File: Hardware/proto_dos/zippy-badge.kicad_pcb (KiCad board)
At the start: 2 copper layers, 98 x 104 mm, 90 parts, among them J1 Micro_SD_Card_SPI, J2 USB-C, SW1 Boot Select, SW2 SW_SPDT, U1 NCP115ASN330T2G, U2 RP2040, U3 W25Q32RV, X1 Badgelife_sao_connector_v169b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, Y1 ABM8-272-T3

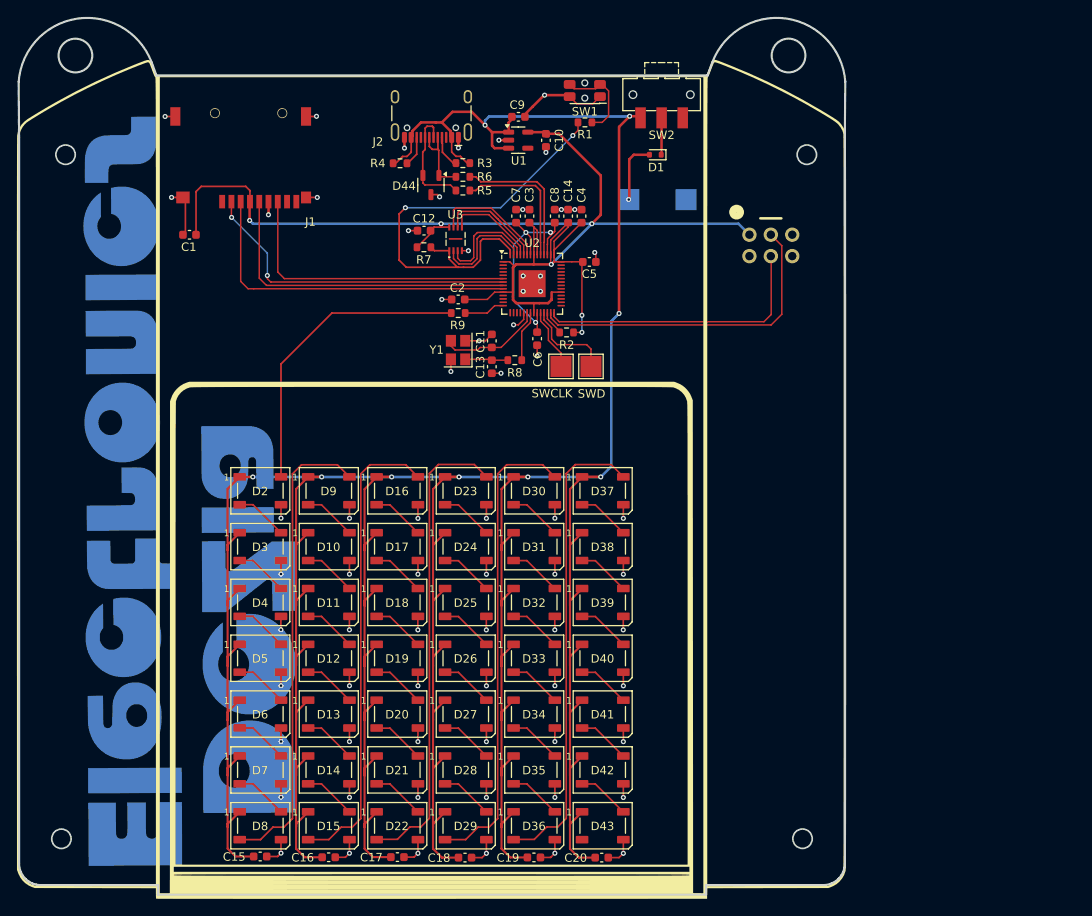
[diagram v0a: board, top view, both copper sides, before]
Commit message: Updated schematic to add Flipper Zero GPIO pinout Modified pin out of RP2040 to make for better routing Update of PCB to add new parts and test layout
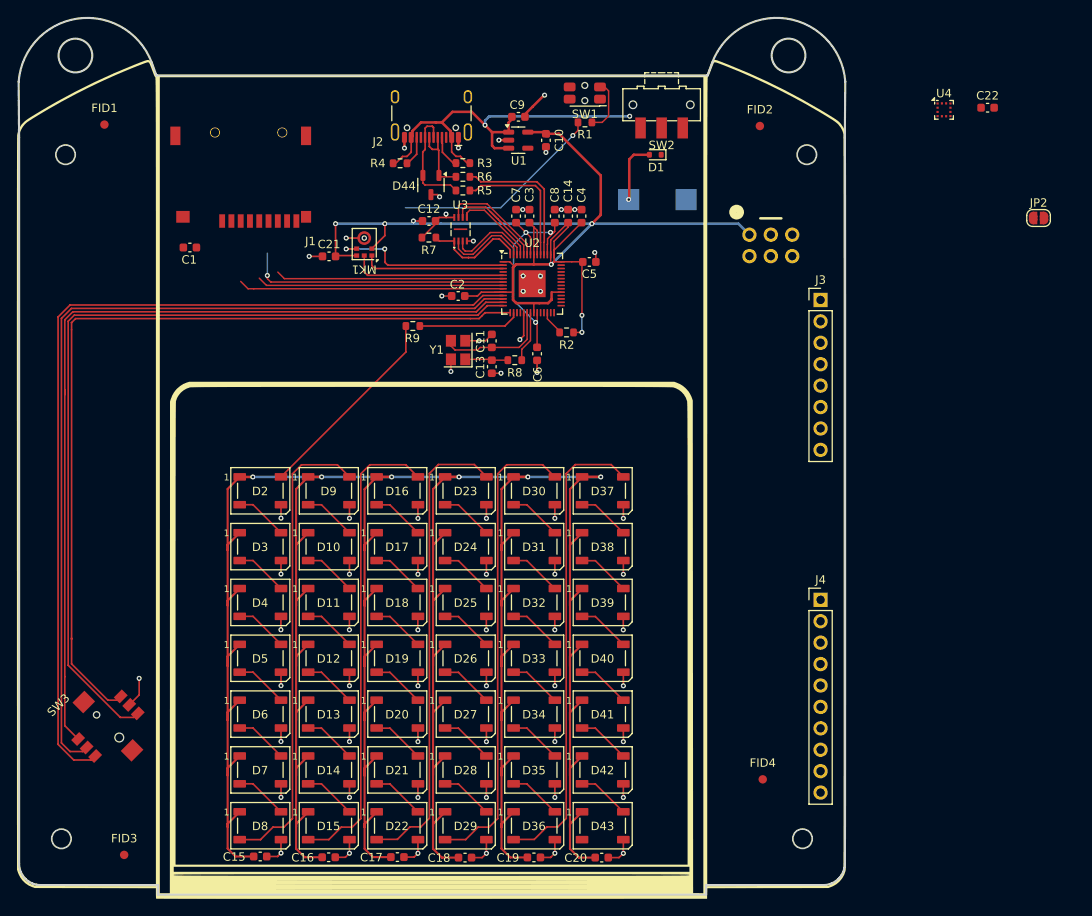
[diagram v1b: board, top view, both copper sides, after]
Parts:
- removed the G*** at (133.9, 91.4)
- removed TP3: SWCLK, TestPoint:TestPoint_Pad_2.5x2.5mm
- removed TP4: SWD, TestPoint:TestPoint_Pad_2.5x2.5mm
- added C21: 0.1uF, Capacitor_SMD:C_0603_1608Metric, F.Cu at (118.2, 63.3)
- added C22: 0.1uF, Capacitor_SMD:C_0603_1608Metric, F.Cu at (196.3, 45.6)
- added FID1: Fiducial, Fiducial:Fiducial_1mm_Mask2mm, F.Cu at (91.5, 47.6)
- added FID2: Fiducial, Fiducial:Fiducial_1mm_Mask2mm, F.Cu at (169.3, 47.8)
- added FID3: Fiducial, Fiducial:Fiducial_1mm_Mask2mm, F.Cu at (93.9, 134.2)
- added FID4: Fiducial, Fiducial:Fiducial_1mm_Mask2mm, F.Cu at (169.6, 125.3)
- added J3: Conn_01x08, Connector_PinHeader_2.54mm:PinHeader_1x08_P2.54mm_Vertical, F.Cu at (176.5, 68.4)
- added J4: Conn_01x10, Connector_PinHeader_2.54mm:PinHeader_1x10_P2.54mm_Vertical, F.Cu at (176.5, 104.0)
- added JP2: SolderJumper_2_Open, Jumper:SolderJumper-2_P1.3mm_Open_RoundedPad1.0x1.5mm, F.Cu at (202.3, 58.7)
- added MK1: ICS-43434, Sensor_Audio:InvenSense_ICS-43434-6_3.5x2.65mm, F.Cu at (122.3, 61.8)
- added SW3: SKRHABE010, lib_fp:SKRHABE010, F.Cu at (91.9, 119.0)
- added U4: GSDA213, Package_LGA:Kionix_LGA-12_2x2mm_P0.5mm_LayoutBorder2x4y, F.Cu at (191.1, 45.9)
- moved R9 5.60 mm to (128.1, 71.5)
- moved J1 2.30 mm to (107.7, 48.6)
- moved C6 1.80 mm to (142.8, 74.8)
- moved C1 1.51 mm to (101.7, 62.2)
- moved R7 1.29 mm to (130.0, 61.0)
- moved C12 1.29 mm to (130.0, 59.1)
- moved U3 1.29 mm to (133.8, 60.1)
- moved SW2 1.20 mm to (157.6, 45.3)
- moved C2 0.41 mm to (133.5, 68.0)
- moved SW1 0.30 mm to (148.5, 43.9)
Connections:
- net Net-(U2-XIN) renamed XTAL_IN
- net Net-(U2-XOUT) renamed XTAL_OUT
- J2 pad A6: Net-(D44-K-Pad2) -> Net-(D44-K-Pad1)
- J2 pad A7: Net-(D44-K-Pad1) -> Net-(D44-K-Pad2)
- J2 pad B6: Net-(D44-K-Pad2) -> Net-(D44-K-Pad1)
- J2 pad B7: Net-(D44-K-Pad1) -> Net-(D44-K-Pad2)
- R3 pad 2: VBUS -> GND
- R4 pad 2: VBUS -> GND
- R5 pad 2: /USB_P -> USB_N
- R6 pad 1: /USB_N -> USB_P
- U2 pad 11: unconnected-(U2-GPIO8-Pad11) -> DPAD_C
- U2 pad 12: unconnected-(U2-GPIO9-Pad12) -> DPAD_CTR
- U2 pad 13: unconnected-(U2-GPIO10-Pad13) -> DPAD_A
- U2 pad 14: RGB -> DPAD_D
- U2 pad 15: unconnected-(U2-GPIO12-Pad15) -> DPAD_B
- U2 pad 16: unconnected-(U2-GPIO13-Pad16) -> RGB
- U2 pad 2: unconnected-(U2-GPIO0-Pad2) -> I2S_BCLK
- U2 pad 24: Net-(U2-SWCLK) -> SWCLK
- U2 pad 25: Net-(U2-SWD) -> SWD
- U2 pad 27: SDA -> GPIO16
- U2 pad 28: SCL -> GPIO17
- U2 pad 29: unconnected-(U2-GPIO18-Pad29) -> GPIO18
- U2 pad 3: unconnected-(U2-GPIO1-Pad3) -> I2S_LRCLK
- U2 pad 30: unconnected-(U2-GPIO19-Pad30) -> GPIO19
- U2 pad 31: unconnected-(U2-GPIO20-Pad31) -> GPIO20
- U2 pad 32: unconnected-(U2-GPIO21-Pad32) -> GPIO21
- U2 pad 34: unconnected-(U2-GPIO22-Pad34) -> SDA
- U2 pad 35: unconnected-(U2-GPIO23-Pad35) -> SCL
- U2 pad 36: unconnected-(U2-GPIO24-Pad36) -> GPIO24
- U2 pad 37: unconnected-(U2-GPIO25-Pad37) -> GPIO25
- U2 pad 38: unconnected-(U2-GPIO26_ADC0-Pad38) -> GPIO26
- U2 pad 39: unconnected-(U2-GPIO27_ADC1-Pad39) -> GPIO27
- U2 pad 40: unconnected-(U2-GPIO28_ADC2-Pad40) -> GPIO28
- U2 pad 41: unconnected-(U2-GPIO29_ADC3-Pad41) -> GPIO29
- U2 pad 46: /USB_N -> USB_N
- U2 pad 47: /USB_P -> USB_P
- U2 pad 5: unconnected-(U2-GPIO3-Pad5) -> I2S_DOUT
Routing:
- net DPAD_C: track 0.00 -> 109.9 mm
- net DPAD_CTR: track 0.00 -> 107.3 mm
- net DPAD_D: track 0.00 -> 104.2 mm
- net DPAD_A: track 0.00 -> 103.8 mm
- net DPAD_B: track 0.00 -> 100.9 mm
- net VBUS: track 534.2 -> 488.7 mm, vias 9 -> 8
- net SDA: track 38.9 -> 0.00 mm
- net SCL: track 33.8 -> 0.06 mm
- net (no net): track 0.00 -> 33.7 mm
- net I2S_BCLK: track 0.00 -> 21.6 mm, vias 0 -> 2
- net I2S_DOUT: track 0.00 -> 18.6 mm
- net /USB_N: track 17.2 -> 0.00 mm
- net I2S_LRCLK: track 0.00 -> 16.9 mm
- net /USB_P: track 16.5 -> 0.00 mm
- net SS: track 53.9 -> 37.6 mm, vias 2 -> 1
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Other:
- board text removed: "SWCLK"
- board text removed: "SWD"

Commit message: Updating artwork outlines to remove complexity at the bottom Adding 3D files for parts Adding STEP file for board Adding SolidWorks assembly for badge with shell
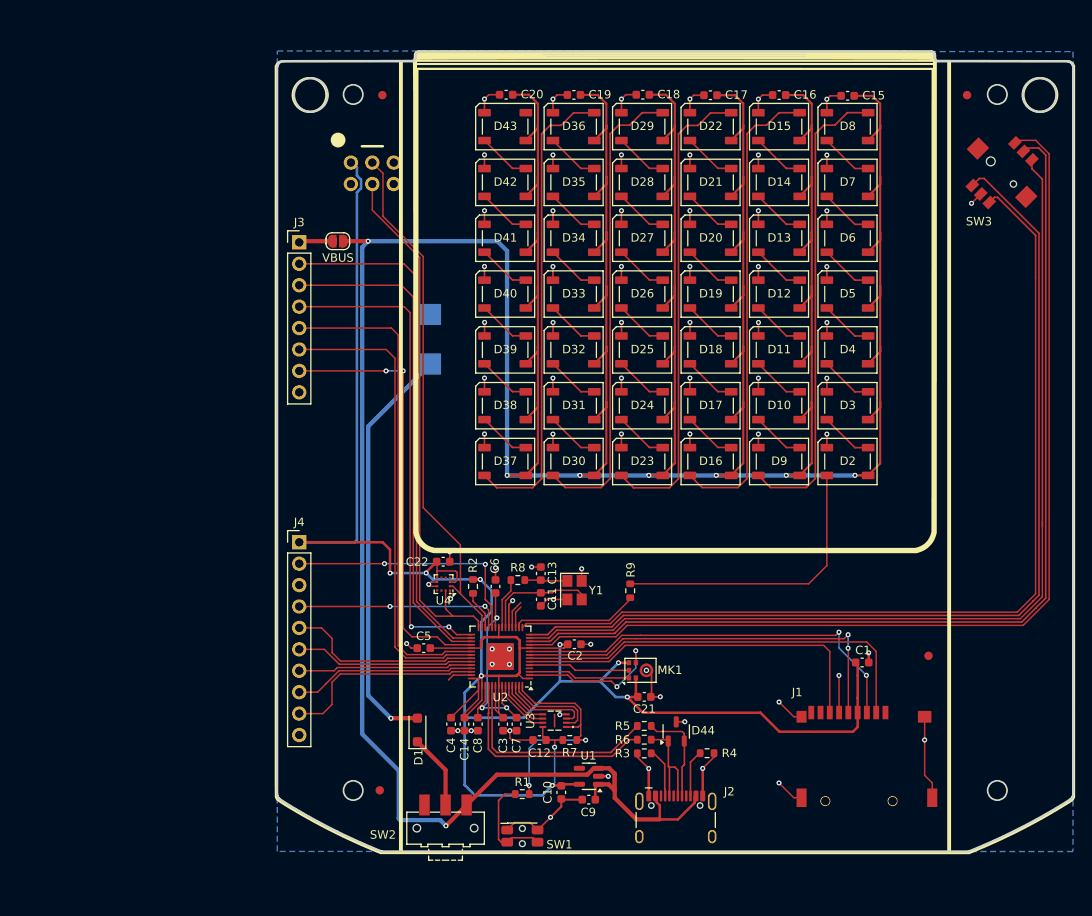
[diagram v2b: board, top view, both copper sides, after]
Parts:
- removed the G*** at (130.1, 86.3)
- removed the G*** at (130.6, 86.2)
- added G***: LOGO, lib_fp:Front Silk 2, F.Cu at (159.0, 82.7)
- D1: footprint Diode_SMD:D_SOD-523 -> Diode_SMD:D_SOD-123F
- D10, D11, D12, D13, D14, D15, D16, D17, D18, D19, D2, D20, D21, D22, D23, D24, D25, D26, D27, D28, D29, D3, D30, D31, D32, D33, D34, D35, D36, D37, D38, D39, D4, D40, D41, D42, D43, D5, D6, D7, D8, D9: footprint LED_SMD:LED_WS2812B_PLCC4_5.0x5.0mm_P3.2mm -> lib_fp:LED_WS2812B_PLCC4_5.0x5.0mm_P3.2mm_Update
- moved FID3 134.6 mm to (193.8, 44.1), turned to 180 degrees
- moved SW3 124.7 mm to (198.0, 53.3), turned to -135 degrees
- moved FID1 116.3 mm to (189.3, 110.6), turned to 180 degrees
- moved C15 114.0 mm to (179.7, 44.2), turned to 0 degrees
- moved J1 108.6 mm to (182.0, 127.9), turned to 0 degrees
- moved D8 108.3 mm to (179.7, 47.9), turned to 180 degrees
- moved C16 105.0 mm to (171.5, 44.1), turned to 0 degrees
- moved D15 98.6 mm to (171.5, 47.9), turned to 180 degrees
- moved D7 98.5 mm to (179.7, 54.5), turned to 180 degrees
- moved C17 97.7 mm to (163.4, 44.2), turned to 0 degrees
- moved C1 93.7 mm to (181.4, 111.4), turned to 180 degrees
- moved C18 92.9 mm to (155.4, 44.1), turned to 0 degrees
- moved FID4 92.8 mm to (124.5, 44.1), turned to 180 degrees
- moved C20 91.2 mm to (139.2, 44.1), turned to 0 degrees
- moved D22 90.9 mm to (163.4, 47.9), turned to 180 degrees
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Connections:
- J2 pad A6: Net-(D44-K-Pad1) -> Net-(D44-K-Pad2)
- J2 pad A7: Net-(D44-K-Pad2) -> Net-(D44-K-Pad1)
- J2 pad B6: Net-(D44-K-Pad1) -> Net-(D44-K-Pad2)
- J2 pad B7: Net-(D44-K-Pad2) -> Net-(D44-K-Pad1)
- J3 pad 2: GPIO27 -> GPIO19
- J3 pad 3: GPIO28 -> GPIO20
- J3 pad 4: GPIO29 -> GPIO18
- J3 pad 5: GPIO26 -> GPIO22
- J3 pad 6: GPIO25 -> GPIO23
- J3 pad 7: GPIO24 -> GPIO21
- J4 pad 5: GPIO20 -> GPIO24
- J4 pad 6: GPIO21 -> GPIO25
- J4 pad 7: GPIO16 -> GPIO26
- J4 pad 8: GPIO17 -> GPIO27
- J4 pad 9: GPIO18 -> GPIO28
- R5 pad 2: USB_N -> USB_P
- R6 pad 1: USB_P -> USB_N
- U2 pad 27: GPIO16 -> SDA
- U2 pad 28: GPIO17 -> SCL
- U2 pad 34: SDA -> GPIO22
- U2 pad 35: SCL -> GPIO23
- U2 pad 41: GPIO29 -> unconnected-(U2-GPIO29_ADC3-Pad41)
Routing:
- net VBUS: track 488.7 -> 654.8 mm
- net +3.3V: track 152.9 -> 263.1 mm, vias 7 -> 9
- net SCL: track 0.06 -> 63.8 mm
- net SDA: track 0.00 -> 62.1 mm
- net GPIO19: track 0.00 -> 61.4 mm
- net GPIO20: track 0.00 -> 59.2 mm
- net GPIO18: track 0.00 -> 58.3 mm, vias 0 -> 2
- net GPIO22: track 0.00 -> 58.2 mm
- net GPIO23: track 0.00 -> 55.8 mm
- net GPIO21: track 0.00 -> 51.9 mm, vias 0 -> 2
- net GND: track 114.6 -> 162.0 mm, vias 67 -> 72
- net Net-(D1-A): track 7.41 -> 49.3 mm
- net (no net): track 33.7 -> 0.00 mm
- net SWCLK: track 0.00 -> 30.0 mm, vias 0 -> 2
- net USB_N: track 0.00 -> 26.4 mm
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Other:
- board size 98 x 104 mm -> 94.4 x 94.9 mm
- board text added: "BATTERY BOX"

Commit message: Adding artwork to the back Added blocking diode for VBUS Added outputs
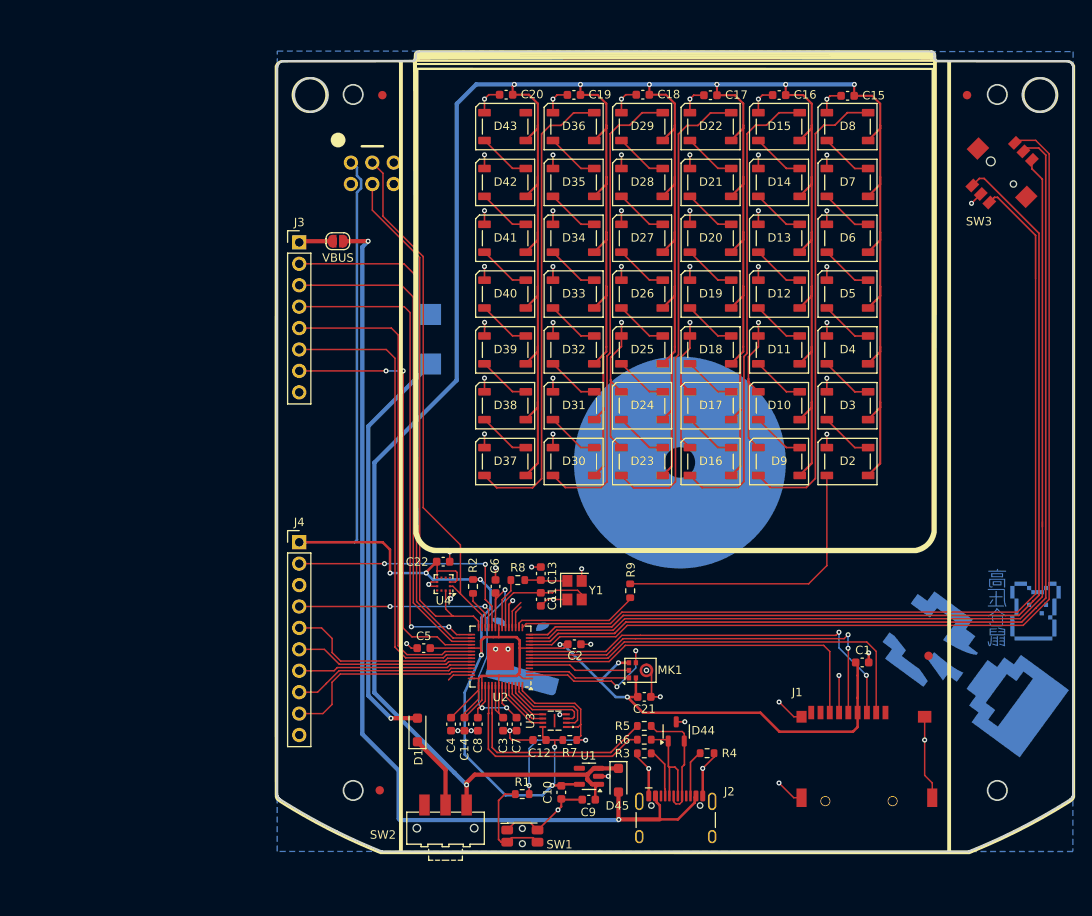
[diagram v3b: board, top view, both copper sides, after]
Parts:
- removed the G*** at (201.0, 118.3)
- added D45: D_Schottky, Diode_SMD:D_SOD-123F, F.Cu at (152.5, 125.4)
- added G***: LOGO, lib_fp:Back Silk, B.Cu at (160.2, 82.7)
- added G***: LOGO, lib_fp:Back Copper, B.Cu at (160.2, 82.7)
- added G***: LOGO, lib_fp:hamster-copper, B.Cu at (200.6, 104.9)
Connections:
- C15 pad 2: VBUS -> VCC
- C16 pad 2: VBUS -> VCC
- C17 pad 2: VBUS -> VCC
- C18 pad 2: VBUS -> VCC
- C19 pad 2: VBUS -> VCC
- C20 pad 2: VBUS -> VCC
- C9 pad 2: VBUS -> VCC
- D10 pad 1: VBUS -> VCC
- D11 pad 1: VBUS -> VCC
- D12 pad 1: VBUS -> VCC
- D13 pad 1: VBUS -> VCC
- D14 pad 1: VBUS -> VCC
- D15 pad 1: VBUS -> VCC
- D16 pad 1: VBUS -> VCC
- D17 pad 1: VBUS -> VCC
- D18 pad 1: VBUS -> VCC
- D19 pad 1: VBUS -> VCC
- D2 pad 1: VBUS -> VCC
- D20 pad 1: VBUS -> VCC
- D21 pad 1: VBUS -> VCC
- D22 pad 1: VBUS -> VCC
- D23 pad 1: VBUS -> VCC
- D24 pad 1: VBUS -> VCC
- D25 pad 1: VBUS -> VCC
- D26 pad 1: VBUS -> VCC
- D27 pad 1: VBUS -> VCC
- D28 pad 1: VBUS -> VCC
- D29 pad 1: VBUS -> VCC
- D3 pad 1: VBUS -> VCC
- D30 pad 1: VBUS -> VCC
- D31 pad 1: VBUS -> VCC
- D32 pad 1: VBUS -> VCC
- D33 pad 1: VBUS -> VCC
- D34 pad 1: VBUS -> VCC
- D35 pad 1: VBUS -> VCC
- D36 pad 1: VBUS -> VCC
- D37 pad 1: VBUS -> VCC
- D38 pad 1: VBUS -> VCC
- D39 pad 1: VBUS -> VCC
- D4 pad 1: VBUS -> VCC
- D40 pad 1: VBUS -> VCC
- D41 pad 1: VBUS -> VCC
- D42 pad 1: VBUS -> VCC
- D43 pad 1: VBUS -> VCC
- D5 pad 1: VBUS -> VCC
- D6 pad 1: VBUS -> VCC
- D7 pad 1: VBUS -> VCC
- D8 pad 1: VBUS -> VCC
- D9 pad 1: VBUS -> VCC
- SW2 pad 3: VBUS -> VCC
- U1 pad 1: VBUS -> VCC
- U1 pad 3: VBUS -> VCC
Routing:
- net VCC: track 0.00 -> 553.1 mm, vias 0 -> 7
- net VBUS: track 654.8 -> 116.7 mm, vias 8 -> 2
- net GND: track 162.0 -> 200.8 mm, vias 72 -> 64
- net +3.3V: track 263.1 -> 245.6 mm
- net Net-(U2-VREG_VOUT): track 28.0 -> 34.2 mm
- net Net-(D44-K-Pad2): track 11.9 -> 14.5 mm
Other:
- board text added: "github.com/dczia"
- board text removed: "BATTERY BOX"

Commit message: Final updates before board order
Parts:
- added TP3: ~, TestPoint:TestPoint_Pad_1.0x1.0mm, F.Cu at (145.9, 112.6)
- added TP4: ~, TestPoint:TestPoint_Pad_1.0x1.0mm, F.Cu at (141.5, 105.5)
- added TP5: ~, TestPoint:TestPoint_Pad_1.0x1.0mm, F.Cu at (141.5, 104.1)
- added TP6: ~, TestPoint:TestPoint_Pad_1.0x1.0mm, F.Cu at (131.1, 114.6)
- moved G*** 5.74 mm to (200.4, 99.2)
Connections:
- U2 pad 17: unconnected-(U2-GPIO14-Pad17) -> Net-(U2-GPIO14)
- U2 pad 18: unconnected-(U2-GPIO15-Pad18) -> Net-(U2-GPIO15)
- U2 pad 4: unconnected-(U2-GPIO2-Pad4) -> Net-(U2-GPIO2)
- U2 pad 41: unconnected-(U2-GPIO29_ADC3-Pad41) -> Net-(U2-GPIO29_ADC3)
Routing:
- net GND: track 200.8 -> 210.6 mm
- net Net-(U2-GPIO29_ADC3): track 0.00 -> 4.66 mm
- net Net-(U2-GPIO15): track 0.00 -> 4.37 mm
- net Net-(U2-GPIO2): track 0.00 -> 4.14 mm
- net unconnected-(U2-GPIO15-Pad18): track 3.39 -> 0.00 mm
- net unconnected-(U2-GPIO29_ADC3-Pad41): track 2.94 -> 0.00 mm
- net Net-(U2-GPIO14): track 0.00 -> 2.75 mm
- net unconnected-(U2-GPIO14-Pad17): track 2.70 -> 0.00 mm
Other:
- board text added: "dczia zippy badge"
- board text added: "not tested on green chile"
- board text added: "v1.1"
- board text removed: "github.com/dczia"
